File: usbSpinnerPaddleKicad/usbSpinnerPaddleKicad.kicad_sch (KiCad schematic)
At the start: 7 parts, among them J1 Conn_01x02_Pin, SW1 RotaryEncoder, SW2 SW_Wuerth_450301014042, U1 RP2040-ZERO

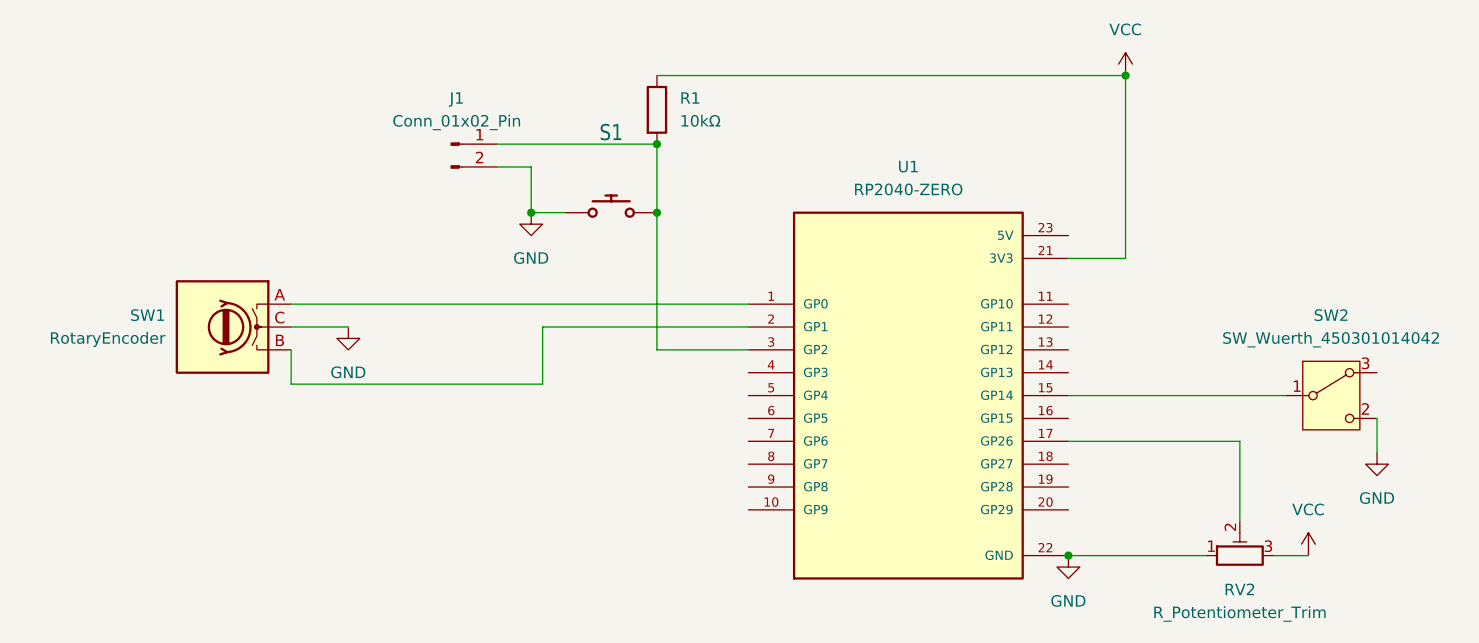
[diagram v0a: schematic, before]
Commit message: schematic update
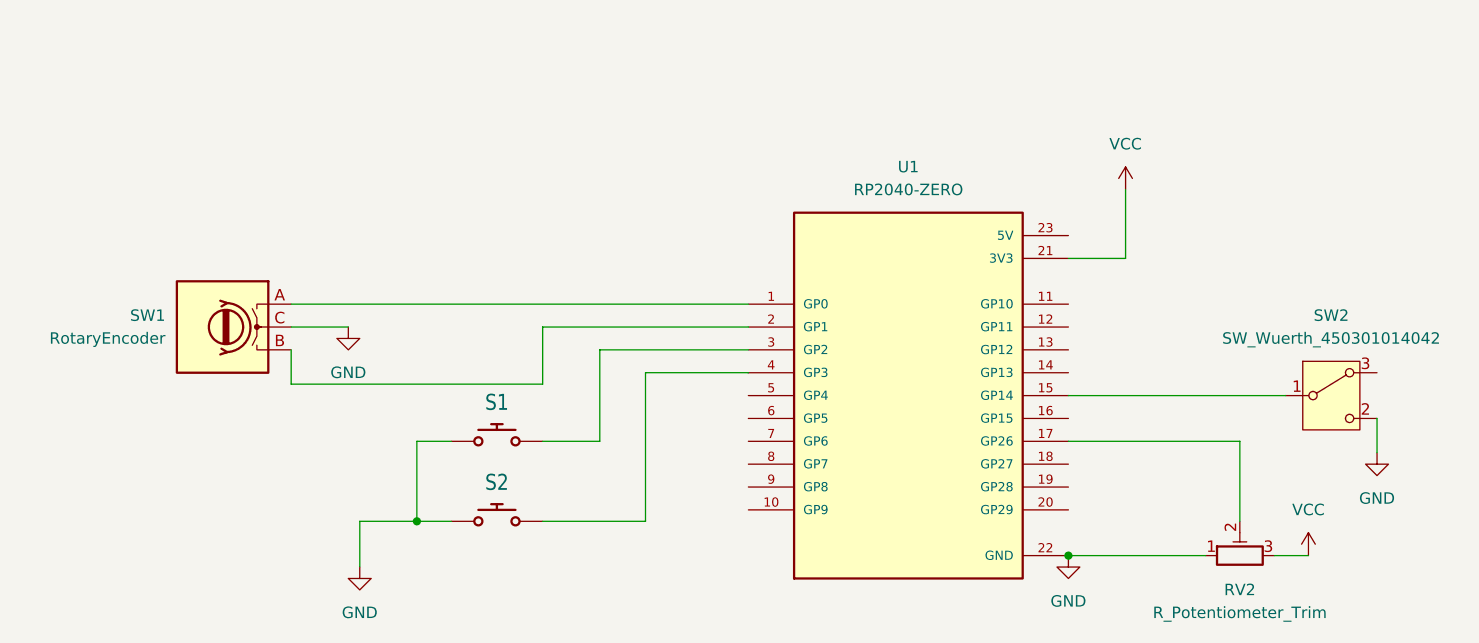
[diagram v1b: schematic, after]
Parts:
- removed J1: Conn_01x02_Pin, Connector_PinHeader_2.54mm:PinHeader_1x02_P2.54mm_Vertical, symbol Connector:Conn_01x02_Pin
- removed R1: 10kΩ, Resistor_THT:R_Axial_DIN0309_L9.0mm_D3.2mm_P12.70mm_Horizontal, symbol Device:R
- added S2: (no value), Button_Switch_Keyboard:SW_Cherry_MX_1.00u_Plate, symbol gpad1:CHERRY_MX
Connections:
- net GND: now also S2.1
- net at U1.4 (GP3): now also S2.2
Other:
- moved on the sheet: S1

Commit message: spinner edits for clarity
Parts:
- RV2: value R_Potentiometer_Trim -> 10KΩ Linear
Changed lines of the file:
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@@
 			)
 		)
-		(property "Value" "R_Potentiometer_Trim"
+		(property "Value" "10KΩ Linear"
 			(at 165.1 119.38 90)
 			(show_name no)
